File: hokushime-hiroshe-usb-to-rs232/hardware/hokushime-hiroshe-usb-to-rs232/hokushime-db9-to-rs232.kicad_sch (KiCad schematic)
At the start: 6 parts, among them IC1 SP3243EC/EB, U1 FT232BM/BL, U2 AT24CS02-SSHM

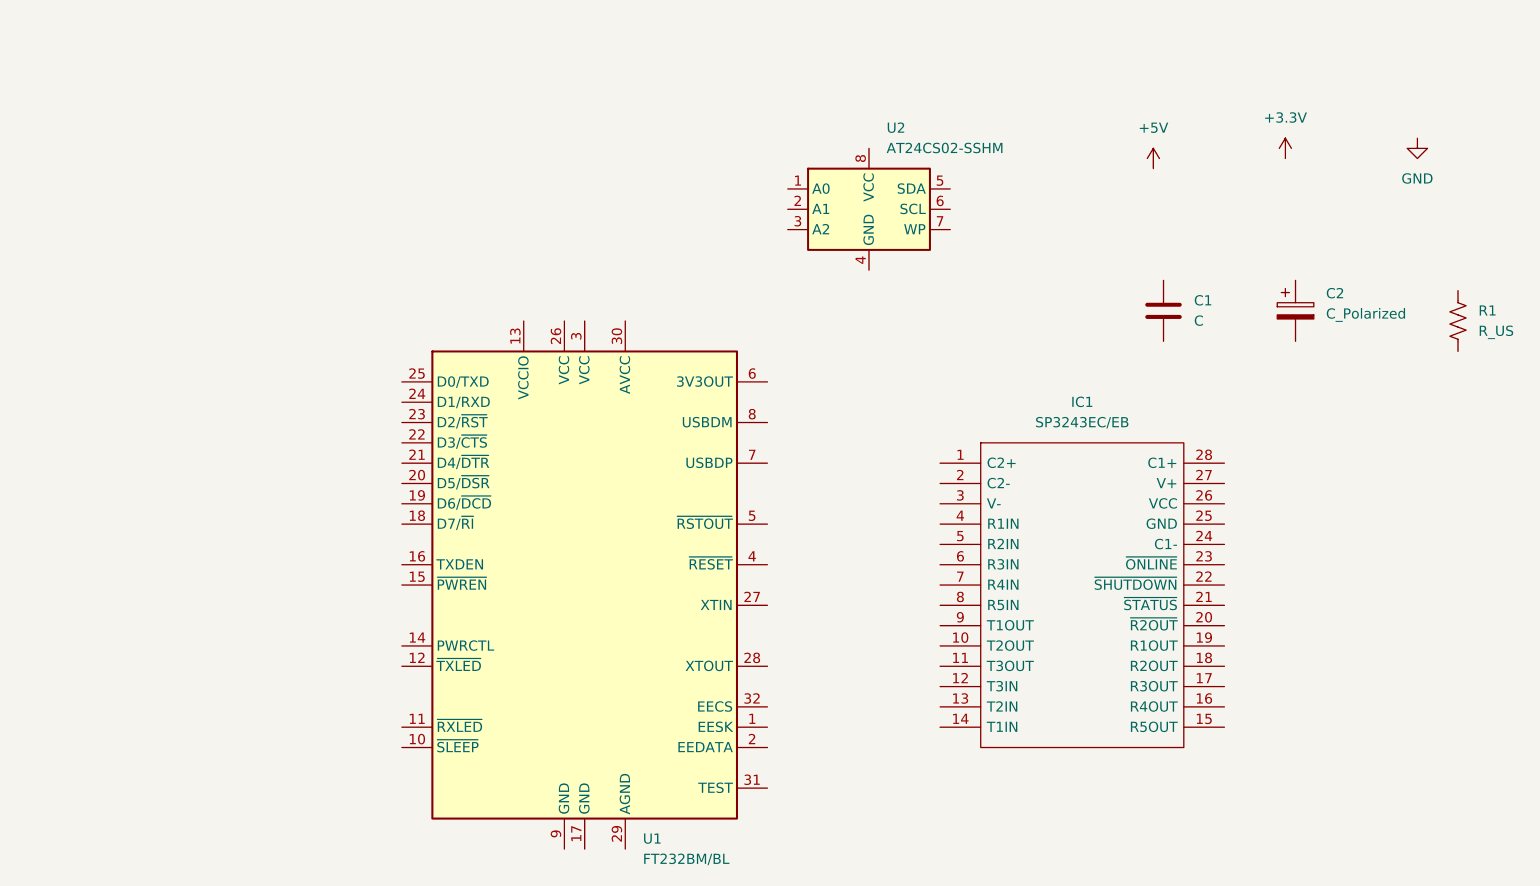
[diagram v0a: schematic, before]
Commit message: [04-15-0702] change to use ic 93CXX
nit
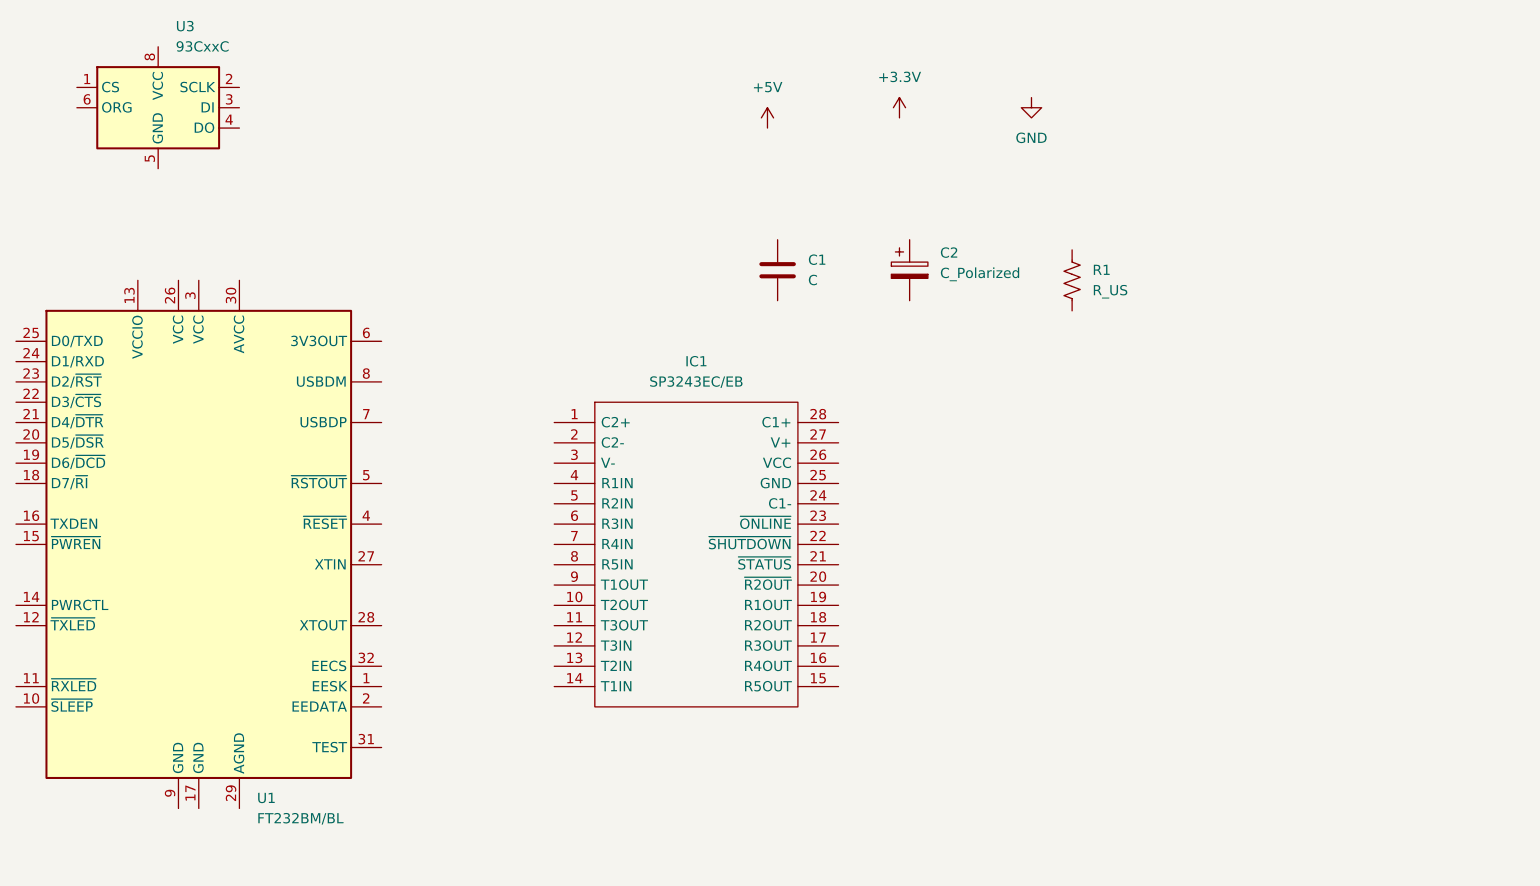
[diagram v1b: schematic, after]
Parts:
- removed U2: AT24CS02-SSHM, Package_SO:SOIC-8_3.9x4.9mm_P1.27mm, symbol Memory_EEPROM:AT24CS02-SSHM
- added U3: 93CxxC, Package_SO:SOIC-8_3.9x4.9mm_P1.27mm, symbol Memory_EEPROM:93CxxC
- C1, C2: footprint (none) -> Capacitor_SMD:C_0603_1608Metric_Pad1.08x0.95mm_HandSolder
- IC1: footprint SOP65P780X200-28N -> Package_SO:TSSOP-28_4.4x9.7mm_P0.65mm
- R1: footprint (none) -> Resistor_SMD:R_0805_2012Metric_Pad1.20x1.40mm_HandSolder
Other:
- moved on the sheet: C1, C2, IC1, R1, U1

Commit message: [04-15-2111] finish first schematic
Update README.md

Update README.md
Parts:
- added C3: 27pF, Capacitor_SMD:C_0603_1608Metric_Pad1.08x0.95mm_HandSolder, symbol Device:C
- added C4: 0.1uF, Capacitor_SMD:C_0603_1608Metric_Pad1.08x0.95mm_HandSolder, symbol Device:C
- added C5: 33nF, Capacitor_SMD:C_0603_1608Metric_Pad1.08x0.95mm_HandSolder, symbol Device:C
- added C6, C7, C8, C9: 0.22uF/16V, Capacitor_SMD:C_0603_1608Metric_Pad1.08x0.95mm_HandSolder, symbol Device:C_Polarized
- added FB1: 40 Ohms @100 MHz, Inductor_SMD:L_0603_1608Metric_Pad1.05x0.95mm_HandSolder, symbol Device:FerriteBead_Small
- added J1: Conn1, symbol Connector_Generic:Conn_01x07
- added J2: USB_B, Connector_USB:USB_B_Lumberg_2411_02_Horizontal, symbol Connector:USB_B
- added J3: Conn2, symbol Connector_Generic:Conn_01x10
- added JP1: 5V-1, Test-2, GND-3, Jumper:SolderJumper-3_P2.0mm_Open_TrianglePad1.0x1.5mm_NumberLabels, symbol Jumper:SolderJumper_3_Open
- added JP2: CONN2_TO_GND, symbol Jumper:SolderJumper_2_Open
- added JP3: CONN1_SHIELD_TO_GND, symbol Jumper:SolderJumper_2_Open
- added R2: 2K2, Resistor_SMD:R_0805_2012Metric_Pad1.20x1.40mm_HandSolder, symbol Device:R_US
- added R3, R4: 27, Resistor_SMD:R_0805_2012Metric_Pad1.20x1.40mm_HandSolder, symbol Device:R_US
- added R5: 470, Resistor_SMD:R_0805_2012Metric_Pad1.20x1.40mm_HandSolder, symbol Device:R_US
- added R6: 1K5, Resistor_SMD:R_0805_2012Metric_Pad1.20x1.40mm_HandSolder, symbol Device:R_US
- added TP1: Status, TestPoint:TestPoint_Pad_D3.0mm, symbol Connector:TestPoint
- added Y1: 6Mhz, symbol Device:Crystal
- C1: value C -> 27pF
- C2: value C_Polarized -> 0.22uF/16V
- R1: value R_US -> 10K
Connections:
- net +5V: now also IC1.26 (VCC), R1.1, U1.13 (VCCIO), U1.26 (VCC), U1.3 (VCC), U1.4 (~{RESET}), U3.6 (ORG), U3.8 (VCC), C6.1, FB1.2, JP1.1 (A), R5.2
- net GND: now also C1.2, IC1.23 (~{ONLINE}), IC1.25 (GND), U1.14 (PWRCTL), U1.17 (GND), U1.29 (AGND), U1.9 (GND), U3.5 (GND), C3.2, C4.1, C5.1, C6.2, C7.2, C9.1, J1.5 (Pin_5), J1.6 (Pin_6), J2.4 (GND), J2.5 (Shield), JP1.3 (B), JP2.2 (B), JP3.1 (A)
- net at IC1.1 (C2+): now also C8.1
- net CONN2_RTS: now reaches IC1.10 (T2OUT)
- net CONN2_RTS: now also J3.8 (Pin_8)
- net CONN2_DTR: now reaches IC1.11 (T3OUT)
- net CONN2_DTR: now also J3.1 (Pin_1)
- net ~{DTR}: now reaches IC1.12 (T3IN)
- net ~{DTR}: now also U1.21 (D4/~{DTR})
- net ~{RTS}: now reaches IC1.13 (T2IN)
- net ~{RTS}: now also U1.23 (D2/~{RST})
- net TXD: now reaches IC1.14 (T1IN)
- net TXD: now also U1.25 (D0/TXD)
- net ~{RI}: now reaches IC1.15 (R5OUT)
- net ~{RI}: now also U1.18 (D7/~{RI})
- net ~{DCD}: now reaches IC1.16 (R4OUT)
- net ~{DCD}: now also U1.19 (D6/~{DCD})
- net ~{DSR}: now reaches IC1.17 (R3OUT)
- net ~{DSR}: now also U1.20 (D5/~{DSR})
- net ~{CTS}: now reaches IC1.18 (R2OUT)
- net ~{CTS}: now also U1.22 (D3/~{CTS})
- net RXD: now reaches IC1.19 (R1OUT)
- net RXD: now also U1.24 (D1/RXD)
- net at IC1.2 (C2-): now also C8.2
- net at IC1.21 (~{STATUS}): now also TP1.1
- net ~{SLEEP}: now reaches IC1.22 (~{SHUTDOWN})
- net ~{SLEEP}: now also U1.10 (~{SLEEP})
- net at IC1.24 (C1-): now also C2.2
- net at IC1.27 (V+): now also C7.1
- net at IC1.28 (C1+): now also C2.1
- net at IC1.3 (V-): now also C9.2
- net CONN2_RXD: now reaches IC1.4 (R1IN)
- net CONN2_RXD: now also J3.3 (Pin_3)
- net CONN2_CTS: now reaches IC1.5 (R2IN)
- net CONN2_CTS: now also J3.7 (Pin_7)
- net CONN2_DSR: now reaches IC1.6 (R3IN)
- net CONN2_DSR: now also J3.4 (Pin_4)
- net CONN2_DCD: now reaches IC1.7 (R4IN)
- net CONN2_DCD: now also J3.6 (Pin_6)
- net CONN2_RI: now reaches IC1.8 (R5IN)
- net CONN2_RI: now also J3.9 (Pin_9)
- net CONN2_TXD: now reaches IC1.9 (T1OUT)
- net CONN2_TXD: now also J3.2 (Pin_2)
- net 93C66_CS: now reaches U3.1 (CS)
- net 93C66_CS: now also U1.32 (EECS)
- net 93C66_SCLK: now reaches U3.2 (SCLK)
- net 93C66_SCLK: now also U1.1 (EESK)
- net 93C66_DI: now reaches U3.3 (DI)
- net 93C66_DI: now also U1.2 (EEDATA), R2.1
- net 93C66_DO: now reaches U3.4 (DO)
- net 93C66_DO: now also R1.2, R2.2
- net at U1.27 (XTIN): now also C1.1, Y1.2
- net at U1.28 (XTOUT): now also C3.1, Y1.1
- net at U1.30 (AVCC): now also C4.2, R5.1
- net at U1.31 (TEST): now also JP1.2 (C)
- net at U1.5 (~{RSTOUT}): now also R6.1
- net at U1.6 (3V3OUT): now also C5.2
- net at U1.7 (USBDP): now also R4.1, R6.2
- net at U1.8 (USBDM): now also R3.1
- new net: J1.7 (Pin_7), JP3.2 (B)
- new net CONN2_GND: J3.5 (Pin_5), JP2.1 (A)
- new net CONN2_SHIELD: J3.10 (Pin_10)
- new net USBD+: J1.1 (Pin_1), J2.3 (D+), R4.2
- new net USBD-: J1.2 (Pin_2), J2.2 (D-), R3.2
- new net VBUS: FB1.1, J1.3 (Pin_3), J2.1 (VBUS)
- no-connect marks 0 -> 1
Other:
- note added: "Black DTR Brown TXD Red RXD Orange DSR Yellow GND Green DCD Blue CTS Gray RTS White RI Braid Shield Look For Green"
- note added: "Connect to GND for normal operation"
- note added: "EEPROM"
- note added: "Hirose 6 pin connector 1 USBD+ GREEN P2 2 USBD- WHITE P1 3 USBVBUS YELLOW P3 5 USB_OTG_ID(GND) PINK P6 6 GND BLACK P5 SHELL SHIELD SHIELD P7"
- note added: "NOTE: What Usage of SHIELD"
- note added: "ORG -> 5V = 16Bit"
- note added: "RS232 to Serial"
- note added: "RTS is typo, Writed RST"
- note added: "Recomended Ferrite Bead from Datasheet: https://www.digikey.com/en/products/detail/laird-signal-integrity-products/MI0805K400R-00/255538"
- note added: "Typical Resistor Values USB 2.0 High-Speed (480 Mbps): 22Ω-33Ω (most common) USB Full-Speed (12 Mbps): 33Ω-56Ω (if needed for EMI control) USB Low-Speed (1.5 Mbps): Sometimes omitted or higher values (~100Ω)."
- note added: "USB OTG ID Note 5V = As Peripheral 0V = As Host"
- note added: "USB to Serial"
- note added: "💦"
- title: Hokushime DB9 to RS232 -> Hokushime USB to RS232
- moved on the sheet: IC1, U1, U3

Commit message: [04-22-0550] Hokushime create pcb and basic layout
Update README.md
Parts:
- added C10, C12: 0.1uF, Capacitor_SMD:C_0603_1608Metric_Pad1.08x0.95mm_HandSolder, symbol Device:C
- added C11: 10uF, Capacitor_SMD:C_0603_1608Metric_Pad1.08x0.95mm_HandSolder, symbol Device:C_Polarized
- added D1: TX, LED_SMD:LED_0805_2012Metric_Pad1.15x1.40mm_HandSolder, symbol Device:LED_Small
- added D2: RX, LED_SMD:LED_0805_2012Metric_Pad1.15x1.40mm_HandSolder, symbol Device:LED_Small
- added R7, R8: 220, Resistor_SMD:R_0805_2012Metric_Pad1.20x1.40mm_HandSolder, symbol Device:R_US
- J1: footprint (none) -> Connector_PinHeader_2.54mm:PinHeader_1x07_P2.54mm_Horizontal
- J3: footprint (none) -> Connector_PinHeader_2.54mm:PinHeader_1x10_P2.54mm_Horizontal
- JP2, JP3: footprint (none) -> Jumper:SolderJumper-2_P1.3mm_Open_RoundedPad1.0x1.5mm
- TP1: footprint TestPoint:TestPoint_Pad_D3.0mm -> TestPoint:TestPoint_Pad_D1.0mm
- Y1: footprint (none) -> Crystal:Crystal_HC49-U_Vertical
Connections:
- net +5V: now also C10.2, C11.1, C12.2, D1.2 (A), D2.2 (A)
- net GND: now also C10.1, C11.2, C12.1
- net at U1.11 (~{RXLED}): now also R8.2
- net at U1.12 (~{TXLED}): now also R7.2
- new net: D1.1 (K), R7.1
- new net: D2.1 (K), R8.1
- no-connect marks 1 -> 2

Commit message: [04-24-1904] pcb routing finished
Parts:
- added H1, H2, H4: MountingHole, MountingHole:MountingHole_3mm, symbol Mechanical:MountingHole
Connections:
- net CONN2_DCD: now also J3.5 (Pin_5); no longer J3.6 (Pin_6)
- net CONN2_DSR: now also J3.6 (Pin_6); no longer J3.4 (Pin_4)
- net CONN2_GND: now also J3.9 (Pin_9); no longer J3.5 (Pin_5)
- net CONN2_RI: now also J3.4 (Pin_4); no longer J3.9 (Pin_9)
- net CONN2_RTS: now also J3.2 (Pin_2); no longer J3.8 (Pin_8)
- net CONN2_RXD: now also J3.8 (Pin_8); no longer J3.3 (Pin_3)
- net CONN2_TXD: now also J3.3 (Pin_3); no longer J3.2 (Pin_2)
- no-connect marks 2 -> 4
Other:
- note added: "TODO: Recheck this annotation ----------- Black DTR Brown TXD Red RXD Orange DSR Yellow GND Green DCD Blue CTS Gray RTS White RI Braid Shield Look For Green"
- note removed: "Black DTR Brown TXD Red RXD Orange DSR Yellow GND Green DCD Blue CTS Gray RTS White RI Braid Shield Look For Green"
